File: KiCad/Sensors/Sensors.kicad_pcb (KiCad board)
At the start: 2 copper layers, 43.2 x 19 mm, 17 parts, among them J1 Conn_02x06_Odd_Even, U1 OPA1641

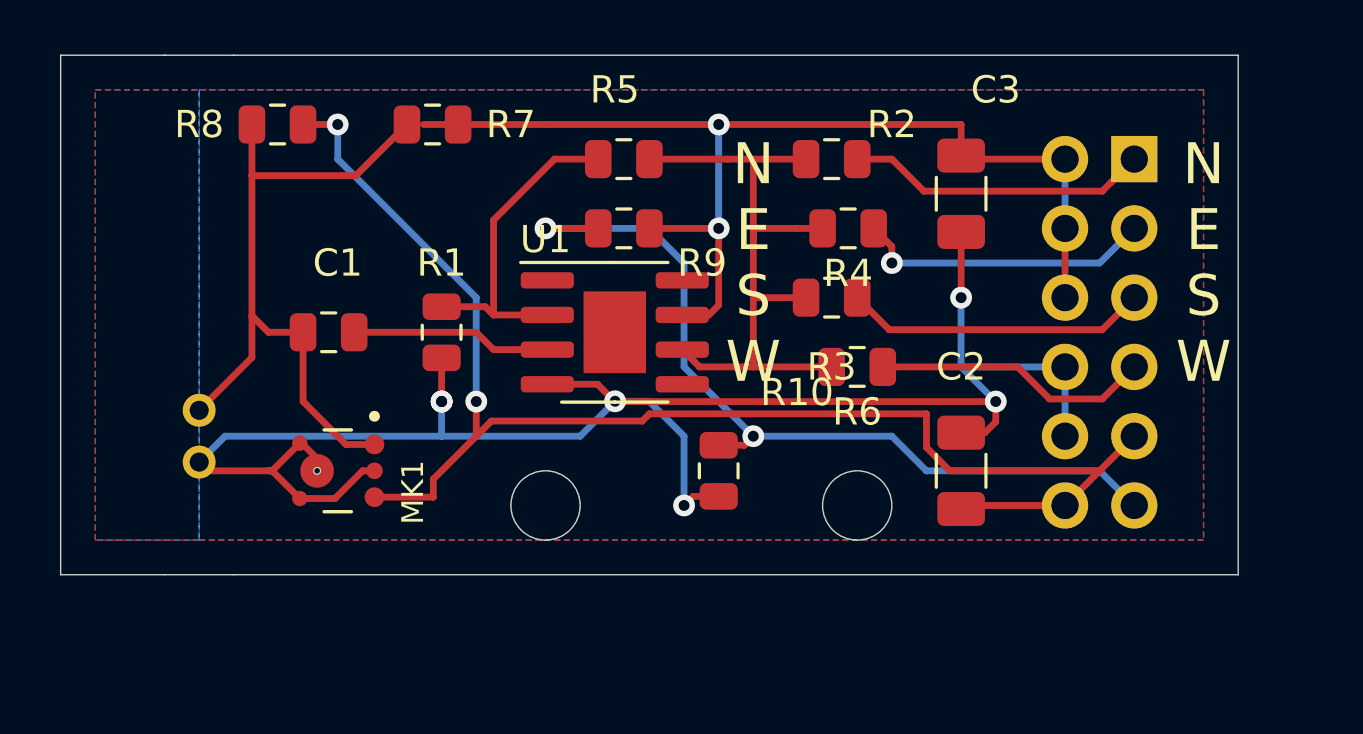
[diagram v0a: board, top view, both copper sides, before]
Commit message: Rewvised Sensor Module
The changes to the sensor module are

Made larger to simplify assembly
Correct routing for negative voltage supply
Moving RTD to the sensor side.
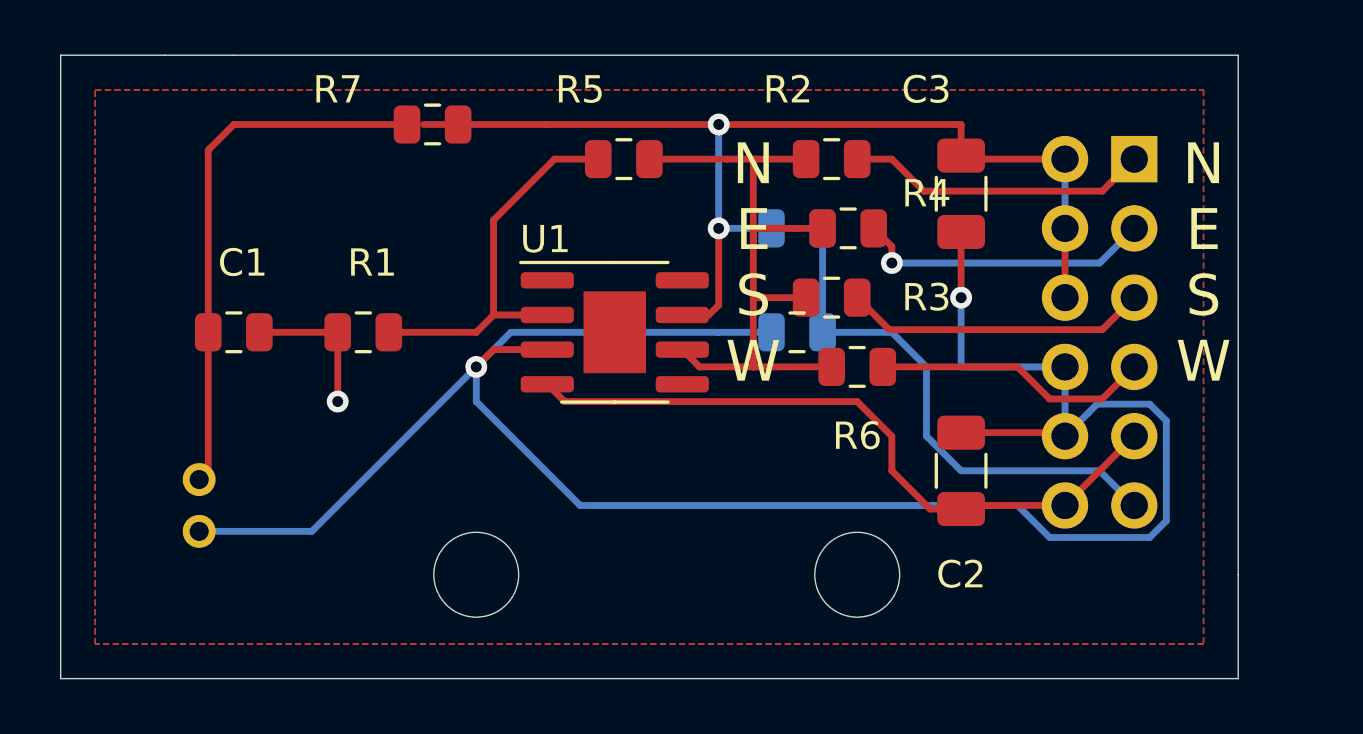
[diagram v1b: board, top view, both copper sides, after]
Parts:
- removed MK1: SPU0410LR5H-QB-7, SnapEDA:MIC_SPU0410LR5H-QB-7
- removed R8: 10K0, Resistor_SMD:R_0805_2012Metric
- R1: value 22r0 -> 2K0
- R5: value 22k0 -> 200K0
- R7: value 10k0 -> 2k2
- R9: moved to B.Cu
- moved R9 6.35 mm to (146.4, 83.8), turned to 0 degrees
- moved R10 5.84 mm to (146.4, 87.6), turned to 180 degrees
- moved C1 3.48 mm to (125.7, 87.6)
- moved R1 2.87 mm to (130.5, 87.6), turned to 180 degrees
- moved MK2 2.54 mm to (123.5, 94.0)
- turned C2 to 270 degrees
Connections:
- C2 pad 1: +3V3 -> GND
- C2 pad 2: GND -> Net-(C2-Pad2)
- J1 pad 12: +3V3 -> Net-(C2-Pad2)
- J1 pad 9: +3V3 -> Net-(C2-Pad2)
- R1 pad 2: GND -> Net-(C1-Pad1)
- U1 pad 3: Net-(C1-Pad1) -> GND
- U1 pad 4: GND -> Net-(C2-Pad2)
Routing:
- net +3V3: track 52.3 -> 0.00 mm, vias 2 -> 0
- net Net-(C2-Pad2): track 0.00 -> 25.5 mm
- net GND: track 68.4 -> 93.7 mm, vias 6 -> 2
- net Net-(J1-Pad11): track 31.4 -> 19.4 mm, vias 2 -> 0
- net Net-(C1-Pad2): track 25.7 -> 19.9 mm
- net Net-(C1-Pad1): track 7.34 -> 5.41 mm, vias 0 -> 1
- net Net-(R1-Pad1): track 12.7 -> 14.3 mm
- net VCC: track 40.7 -> 40.1 mm
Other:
- board size 43.2 x 19 mm -> 43.2 x 22.9 mm

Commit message: Using digital thermometer
Changes to the circuit to support an I2C termometer in place of the RTD
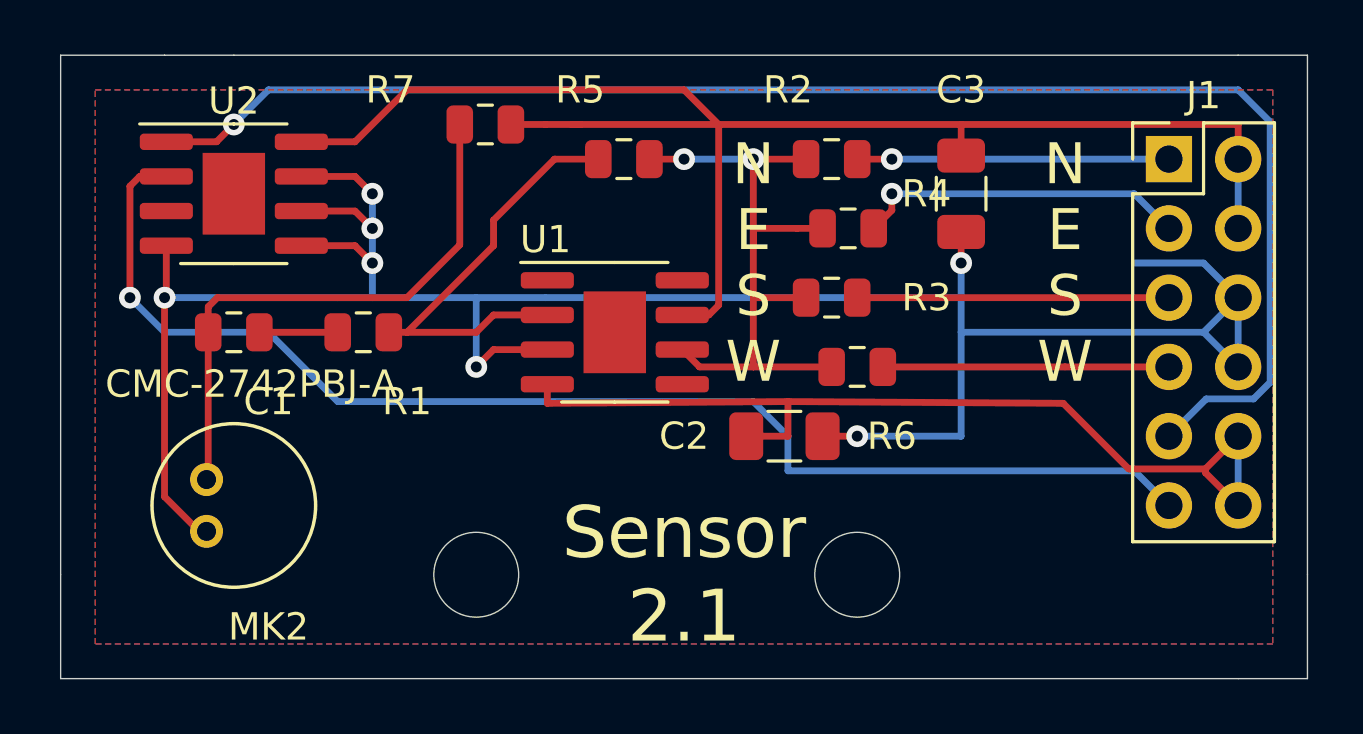
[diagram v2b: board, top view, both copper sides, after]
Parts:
- removed R10: RTRIM, Resistor_SMD:R_0805_2012Metric
- removed R9: 1K0, Resistor_SMD:R_0805_2012Metric
- added U2: LM75AIMX_NOPB, Package_SO:SOIC-8-1EP_3.9x4.9mm_P1.27mm_EP2.29x3mm, F.Cu at (125.7, 82.5)
- J1: value Conn_02x06_Odd_Even -> BERG 2x6; moved to F.Cu
- MK2: moved to F.Cu
- R1: value 2K0 -> 0r
- R5: value 200K0 -> 10K0
- moved C2 6.60 mm to (145.9, 91.4), turned to 180 degrees
- moved MK2 2.27 mm to (125.7, 94.0), turned to 180 degrees
- moved R7 1.93 mm to (135.0, 80.0)
- moved J1 1.27 mm to (160.0, 81.3), turned to 0 degrees
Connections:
- J1 pad 10: GND -> Net-(C2-Pad2)
- J1 pad 6: VCC -> GND
- J1 pad 9: Net-(C2-Pad2) -> Net-(J1-Pad9)
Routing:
- net Net-(J1-Pad9): track 0.00 -> 56.5 mm, vias 0 -> 1
- net Net-(J1-Pad11): track 19.4 -> 47.6 mm, vias 0 -> 1
- net VCC: track 40.1 -> 56.8 mm, vias 2 -> 0
- net Net-(C2-Pad2): track 25.5 -> 34.7 mm
- net GND: track 93.7 -> 90.0 mm, vias 2 -> 7
- net Net-(C1-Pad1): track 5.41 -> 2.87 mm, vias 1 -> 0
- net Net-(R1-Pad1): track 14.3 -> 16.3 mm
- net Net-(J1-Pad3): track 11.0 -> 12.2 mm
- net Net-(C1-Pad2): track 19.9 -> 21.1 mm
- net Net-(J1-Pad1): track 11.1 -> 11.4 mm, vias 0 -> 1
- net Net-(R2-Pad1): vias 0 -> 2
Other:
- board size 43.2 x 22.9 mm -> 45.7 x 22.9 mm
- board text added: "Sensor 2.1"
- board text removed: "Sensor 1.0.X"

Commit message: Changed to I2C Temperature Sensor
The older RTD temperature sensor was replaced by an I2C one located on the main board.

This also brough in changes to the sensor module and additional data on the JSON shot info
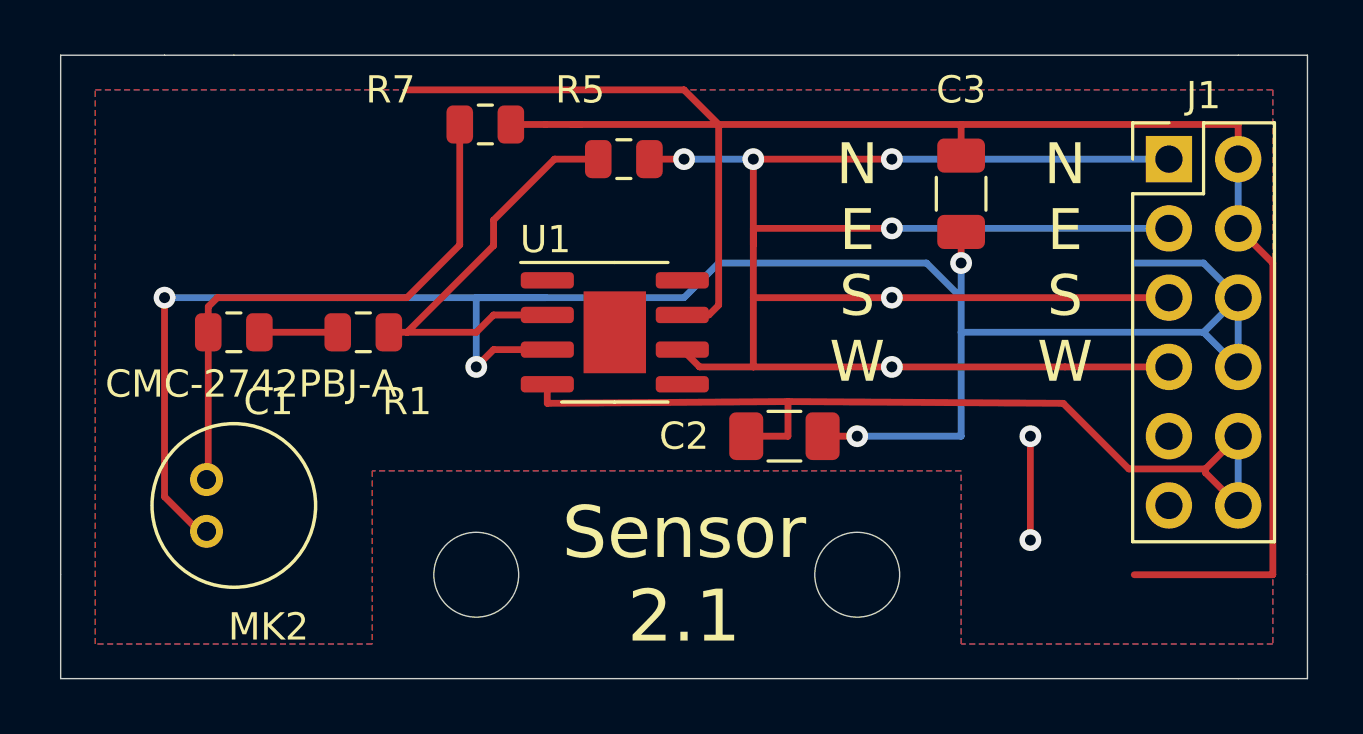
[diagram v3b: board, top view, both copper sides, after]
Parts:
- removed R2, R3, R4, R6: 0r, Resistor_SMD:R_0805_2012Metric
- removed U2: LM75AIMX_NOPB, Package_SO:SOIC-8-1EP_3.9x4.9mm_P1.27mm_EP2.29x3mm
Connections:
- J1 pad 3: Net-(J1-Pad3) -> Net-(J1-Pad1)
- J1 pad 5: Net-(J1-Pad5) -> Net-(J1-Pad1)
- J1 pad 7: Net-(J1-Pad7) -> Net-(J1-Pad1)
- R5 pad 1: Net-(R2-Pad1) -> Net-(J1-Pad1)
- U1 pad 6: Net-(R2-Pad1) -> Net-(J1-Pad1)
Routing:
- net Net-(J1-Pad1): track 11.4 -> 75.9 mm, vias 1 -> 6
- net Net-(J1-Pad9): track 56.5 -> 0.00 mm, vias 1 -> 0
- net Net-(J1-Pad11): track 47.6 -> 0.00 mm, vias 1 -> 0
- net Net-(R2-Pad1): track 24.2 -> 0.00 mm, vias 2 -> 0
- net VCC: track 56.8 -> 70.5 mm
- net Net-(J1-Pad3): track 12.2 -> 0.00 mm, vias 1 -> 0
- net Net-(J1-Pad5): track 11.4 -> 0.00 mm
- net Net-(J1-Pad7): track 10.5 -> 0.00 mm
- net GND: track 90.0 -> 83.1 mm, vias 7 -> 6
